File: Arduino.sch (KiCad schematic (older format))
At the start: 16 parts

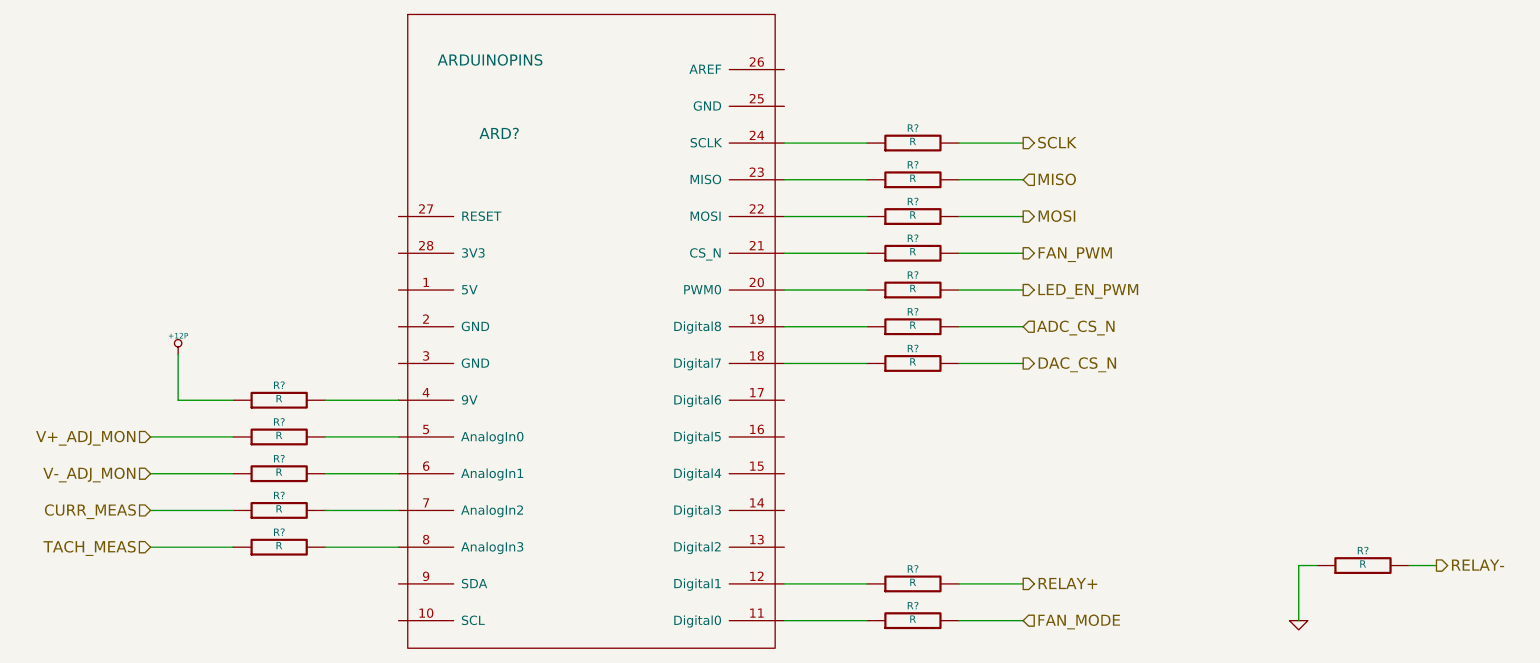
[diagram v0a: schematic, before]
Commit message: Added Relay module footprints.
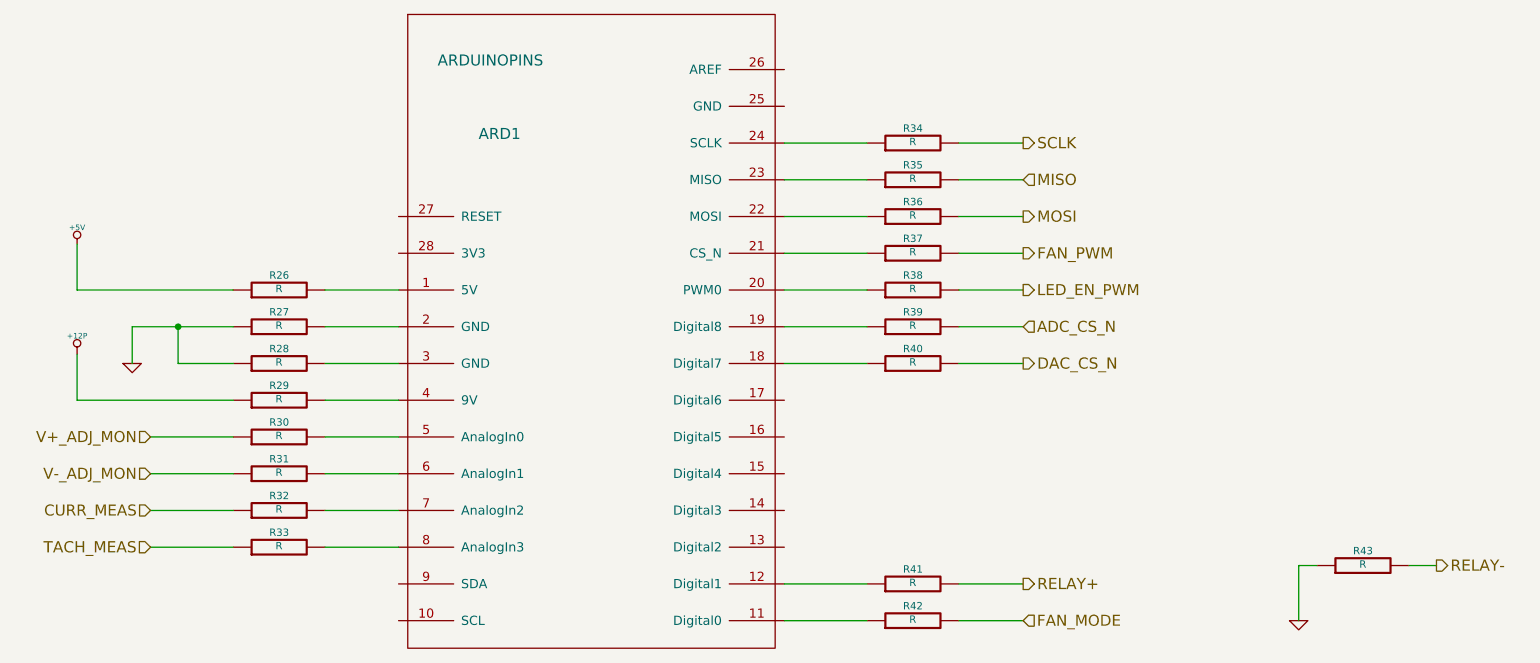
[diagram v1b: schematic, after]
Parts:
- added R26, R27, R28: R, symbol R
- gave numbers to parts that had none: 16
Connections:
- net GND: now also R27.1, R28.1
- net at ARD1.1 (5V): now also R26.2
- net at ARD1.2 (GND): now also R27.2
- net at ARD1.3 (GND): now also R28.2
- new net +5V: R26.1
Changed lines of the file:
@@
 LIBS:valves
 LIBS:BB
+LIBS:GLSP
 LIBS:BB-cache
 EELAYER 24 0
@@
 TACH_MEAS
 $Comp
-L ARDUINOPINS ARD?
+L ARDUINOPINS ARD1
 U 1 1 52F820B7
 P 5000 3950
-F 0 "ARD?" H 4500 5000 60  0000 C CNN
+F 0 "ARD1" H 4500 5000 60  0000 C CNN
 F 1 "ARDUINOPINS" H 4450 5400 60  0000 C CNN
 F 2 "" H 5800 2900 60  0000 C CNN
@@
 CURR_MEAS
 $Comp
-L R R?
+L R R37
 U 1 1 52F82104
 P 6750 3550
-F 0 "R?" V 6830 3550 40  0000 C CNN
+F 0 "R37" V 6830 3550 40  0000 C CNN
 F 1 "R" V 6757 3551 40  0000 C CNN
 F 2 "" V 6680 3550 30  0000 C CNN
@@
 	6500 3550 6050 3550
 $Comp
-L R R?
+L R R41
 U 1 1 52F8212B
 P 6750 5350
-F 0 "R?" V 6830 5350 40  0000 C CNN
+F 0 "R41" V 6830 5350 40  0000 C CNN
 F 1 "R" V 6757 5351 40  0000 C CNN
 F 2 "" V 6680 5350 30  0000 C CNN
@@
 	8850 5250 8850 5550
 $Comp
-L GND #PWR?
+L GND #PWR55
 U 1 1 52F82BF8
 P 8850 5550
-F 0 "#PWR?" H 8850 5550 30  0001 C CNN
+F 0 "#PWR55" H 8850 5550 30  0001 C CNN
 F 1 "GND" H 8850 5480 30  0001 C CNN
 F 2 "" H 8850 5550 60  0000 C CNN
@@
 $EndComp
 $Comp
-L R R?
+L R R33
 U 1 1 52F82E67
 P 3300 5150
-F 0 "R?" V 3380 5150 40  0000 C CNN
+F 0 "R33" V 3380 5150 40  0000 C CNN
 F 1 "R" V 3307 5151 40  0000 C CNN
 F 2 "" V 3230 5150 30  0000 C CNN
@@
 $EndComp
 $Comp
-L R R?
+L R R32
 U 1 1 52F82E72
 P 3300 4950
-F 0 "R?" V 3380 4950 40  0000 C CNN
+F 0 "R32" V 3380 4950 40  0000 C CNN
 F 1 "R" V 3307 4951 40  0000 C CNN
 F 2 "" V 3230 4950 30  0000 C CNN
@@
 V-_ADJ_MON
 $Comp
-L R R?
+L R R31
 U 1 1 52F83112
 P 3300 4750
-F 0 "R?" V 3380 4750 40  0000 C CNN
+F 0 "R31" V 3380 4750 40  0000 C CNN
 F 1 "R" V 3307 4751 40  0000 C CNN
 F 2 "" V 3230 4750 30  0000 C CNN
@@
 $EndComp
 $Comp
-L R R?
+L R R30
 U 1 1 52F8311D
 P 3300 4550
-F 0 "R?" V 3380 4550 40  0000 C CNN
+F 0 "R30" V 3380 4550 40  0000 C CNN
 F 1 "R" V 3307 4551 40  0000 C CNN
 F 2 "" V 3230 4550 30  0000 C CNN
@@
 	2600 4550 3050 4550
 $Comp
-L R R?
+L R R40
 U 1 1 52F833CB
 P 6750 4150
-F 0 "R?" V 6830 4150 40  0000 C CNN
+F 0 "R40" V 6830 4150 40  0000 C CNN
 F 1 "R" V 6757 4151 40  0000 C CNN
 F 2 "" V 6680 4150 30  0000 C CNN
@@
 $EndComp
 $Comp
-L R R?
+L R R36
 U 1 1 52F833D6
 P 6750 3350
-F 0 "R?" V 6830 3350 40  0000 C CNN
+F 0 "R36" V 6830 3350 40  0000 C CNN
 F 1 "R" V 6757 3351 40  0000 C CNN
 F 2 "" V 6680 3350 30  0000 C CNN
@@
 $EndComp
 $Comp
-L R R?
+L R R35
 U 1 1 52F833E1
 P 6750 3150
-F 0 "R?" V 6830 3150 40  0000 C CNN
+F 0 "R35" V 6830 3150 40  0000 C CNN
 F 1 "R" V 6757 3151 40  0000 C CNN
 F 2 "" V 6680 3150 30  0000 C CNN
@@
 $EndComp
 $Comp
-L R R?
+L R R34
 U 1 1 52F833EC
 P 6750 2950
-F 0 "R?" V 6830 2950 40  0000 C CNN
+F 0 "R34" V 6830 2950 40  0000 C CNN
 F 1 "R" V 6757 2951 40  0000 C CNN
 F 2 "" V 6680 2950 30  0000 C CNN
@@
 	6500 4150 6050 4150
 $Comp
-L R R?
+L R R43
 U 1 1 52F83493
 P 9200 5250
-F 0 "R?" V 9280 5250 40  0000 C CNN
+F 0 "R43" V 9280 5250 40  0000 C CNN
 F 1 "R" V 9207 5251 40  0000 C CNN
 F 2 "" V 9130 5250 30  0000 C CNN
@@
 LED_EN_PWM
 $Comp
-L R R?
+L R R38
 U 1 1 52F834CE
 P 6750 3750
-F 0 "R?" V 6830 3750 40  0000 C CNN
+F 0 "R38" V 6830 3750 40  0000 C CNN
 F 1 "R" V 6757 3751 40  0000 C CNN
 F 2 "" V 6680 3750 30  0000 C CNN
@@
 ADC_CS_N
 $Comp
-L R R?
+L R R39
 U 1 1 52F876A6
 P 6750 3950
-F 0 "R?" V 6830 3950 40  0000 C CNN
+F 0 "R39" V 6830 3950 40  0000 C CNN
 F 1 "R" V 6757 3951 40  0000 C CNN
 F 2 "" V 6680 3950 30  0000 C CNN
@@
 FAN_MODE
 $Comp
-L R R?
+L R R42
 U 1 1 52FA1F4F
 P 6750 5550
-F 0 "R?" V 6830 5550 40  0000 C CNN
+F 0 "R42" V 6830 5550 40  0000 C CNN
 F 1 "R" V 6757 5551 40  0000 C CNN
 F 2 "" V 6680 5550 30  0000 C CNN
@@
 	6500 5550 6050 5550
 $Comp
-L R R?
+L R R29
 U 1 1 52FA21F2
 P 3300 4350
-F 0 "R?" V 3380 4350 40  0000 C CNN
+F 0 "R29" V 3380 4350 40  0000 C CNN
 F 1 "R" V 3307 4351 40  0000 C CNN
 F 2 "" V 3230 4350 30  0000 C CNN
@@
 	3950 4350 3550 4350
 $Comp
-L +12P #PWR?
+L +12P #PWR53
 U 1 1 52FA221E
-P 2750 4100
-F 0 "#PWR?" H 2750 4070 30  0001 C CNN
-F 1 "+12P" H 2750 4200 30  0000 C CNN
-F 2 "" H 2750 4100 60  0000 C CNN
-F 3 "" H 2750 4100 60  0000 C CNN
-	1    2750 4100
-	1    0    0    -1
-$EndComp
-Wire Wire Line
-	3050 4350 2750 4350
-Wire Wire Line
-	2750 4350 2750 4100
+P 2200 4100
+F 0 "#PWR53" H 2200 4070 30  0001 C CNN
+F 1 "+12P" H 2200 4200 30  0000 C CNN
+F 2 "" H 2200 4100 60  0000 C CNN
+F 3 "" H 2200 4100 60  0000 C CNN
+	1    2200 4100
+	1    0    0    -1
+$EndComp
+Wire Wire Line
+	3050 4350 2200 4350
+Wire Wire Line
+	2200 4350 2200 4100
+$Comp
+L R R28
+U 1 1 530266F7
+P 3300 4150
+F 0 "R28" V 3380 4150 40  0000 C CNN
+F 1 "R" V 3307 4151 40  0000 C CNN
+F 2 "" V 3230 4150 30  0000 C CNN
+F 3 "" H 3300 4150 30  0000 C CNN
+	1    3300 4150
+	0    -1   -1   0
+$EndComp
+$Comp
+L R R27
+U 1 1 53026702
+P 3300 3950
+F 0 "R27" V 3380 3950 40  0000 C CNN
+F 1 "R" V 3307 3951 40  0000 C CNN
+F 2 "" V 3230 3950 30  0000 C CNN
+F 3 "" H 3300 3950 30  0000 C CNN
+	1    3300 3950
+	0    -1   -1   0
+$EndComp
+$Comp
+L R R26
+U 1 1 5302670D
+P 3300 3750
+F 0 "R26" V 3380 3750 40  0000 C CNN
+F 1 "R" V 3307 3751 40  0000 C CNN
+F 2 "" V 3230 3750 30  0000 C CNN
+F 3 "" H 3300 3750 30  0000 C CNN
+	1    3300 3750
+	0    -1   -1   0
+$EndComp
+Wire Wire Line
+	3950 4150 3550 4150
+Wire Wire Line
+	3950 3950 3550 3950
+Wire Wire Line
+	3950 3750 3550 3750
+Wire Wire Line
+	3050 3750 2200 3750
+Wire Wire Line
+	2200 3750 2200 3500
+$Comp
+L +5V #PWR52
+U 1 1 530267AB
+P 2200 3500
+F 0 "#PWR52" H 2200 3590 20  0001 C CNN
+F 1 "+5V" H 2200 3590 30  0000 C CNN
+F 2 "" H 2200 3500 60  0000 C CNN
+F 3 "" H 2200 3500 60  0000 C CNN
+	1    2200 3500
+	1    0    0    -1
+$EndComp
+Wire Wire Line
+	3050 3950 2500 3950
+Wire Wire Line
+	2500 3950 2500 4150
+$Comp
+L GND #PWR54
+U 1 1 5302681A
+P 2500 4150
+F 0 "#PWR54" H 2500 4150 30  0001 C CNN
+F 1 "GND" H 2500 4080 30  0001 C CNN
+F 2 "" H 2500 4150 60  0000 C CNN
+F 3 "" H 2500 4150 60  0000 C CNN
+	1    2500 4150
+	1    0    0    -1
+$EndComp
+Wire Wire Line
+	3050 4150 2750 4150
+Wire Wire Line
+	2750 4150 2750 3950
+Connection ~ 2750 3950
 $EndSCHEMATC

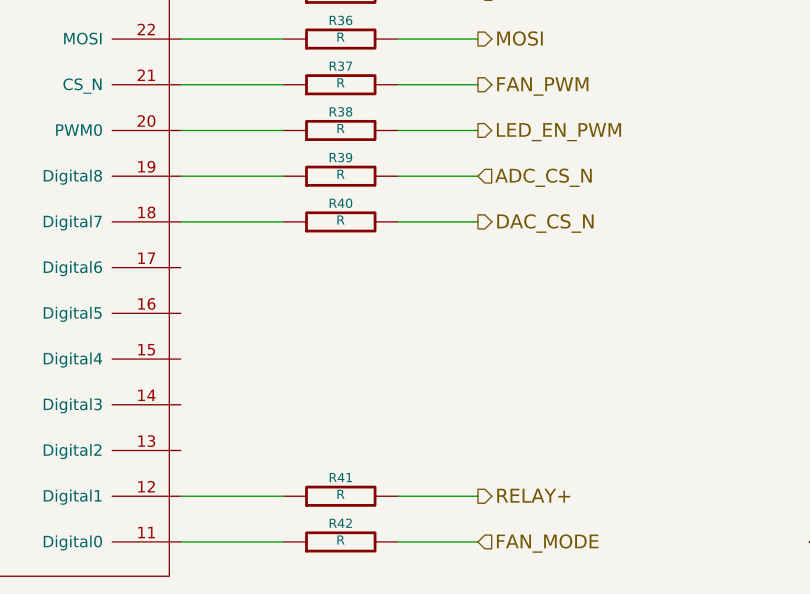
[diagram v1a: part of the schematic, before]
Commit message: Associated and placed thermocouple, terminal, arduino, fan driver, power protection modules.
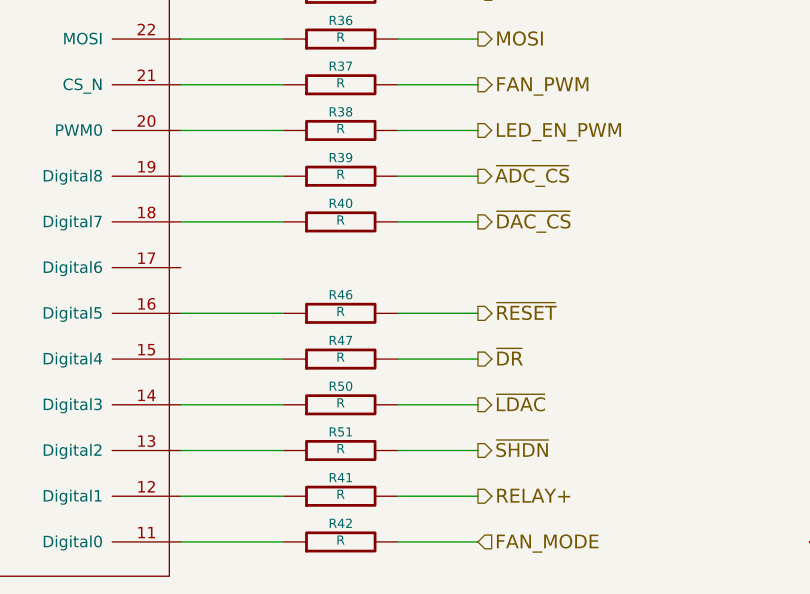
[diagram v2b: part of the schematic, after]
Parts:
- added R46, R47, R50, R51: R, symbol R
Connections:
- net at ARD1.13 (Digital2): now also R51.1
- net at ARD1.14 (Digital3): now also R50.1
- net at ARD1.15 (Digital4): now also R47.1
- net at ARD1.16 (Digital5): now also R46.1
- net ADC_CS_N renamed ~ADC_CS
- net DAC_CS_N renamed ~DAC_CS
- new net ~DR: R47.2
- new net ~LDAC: R50.2
- new net ~RESET: R46.2
- new net ~SHDN: R51.2
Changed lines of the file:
@@
 $Descr A4 11693 8268
 encoding utf-8
-Sheet 9 9
+Sheet 6 9
 Title ""
 Date ""
@@
 SCLK
 Text HLabel 7350 4150 2    61   Output ~ 0
-DAC_CS_N
+~DAC_CS
 Text HLabel 7350 3550 2    61   Output ~ 0
 FAN_PWM
@@
 	8850 5250 8850 5550
 $Comp
-L GND #PWR55
+L GND #PWR048
 U 1 1 52F82BF8
 P 8850 5550
-F 0 "#PWR55" H 8850 5550 30  0001 C CNN
+F 0 "#PWR048" H 8850 5550 30  0001 C CNN
 F 1 "GND" H 8850 5480 30  0001 C CNN
 F 2 "" H 8850 5550 60  0000 C CNN
@@
 Wire Wire Line
 	6500 3750 6050 3750
-Text HLabel 7350 3950 2    60   Input ~ 0
-ADC_CS_N
+Text HLabel 7350 3950 2    60   Output ~ 0
+~ADC_CS
 $Comp
 L R R39
@@
 	3950 4350 3550 4350
 $Comp
-L +12P #PWR53
+L +12P #PWR049
 U 1 1 52FA221E
 P 2200 4100
-F 0 "#PWR53" H 2200 4070 30  0001 C CNN
+F 0 "#PWR049" H 2200 4070 30  0001 C CNN
 F 1 "+12P" H 2200 4200 30  0000 C CNN
 F 2 "" H 2200 4100 60  0000 C CNN
@@
 	2200 3750 2200 3500
 $Comp
-L +5V #PWR52
+L +5V #PWR050
 U 1 1 530267AB
 P 2200 3500
-F 0 "#PWR52" H 2200 3590 20  0001 C CNN
+F 0 "#PWR050" H 2200 3590 20  0001 C CNN
 F 1 "+5V" H 2200 3590 30  0000 C CNN
 F 2 "" H 2200 3500 60  0000 C CNN
@@
 	2500 3950 2500 4150
 $Comp
-L GND #PWR54
+L GND #PWR051
 U 1 1 5302681A
 P 2500 4150
-F 0 "#PWR54" H 2500 4150 30  0001 C CNN
+F 0 "#PWR051" H 2500 4150 30  0001 C CNN
 F 1 "GND" H 2500 4080 30  0001 C CNN
 F 2 "" H 2500 4150 60  0000 C CNN
@@
 	2750 4150 2750 3950
 Connection ~ 2750 3950
+Text HLabel 7350 4550 2    61   Output ~ 0
+~RESET
+$Comp
+L R R46
+U 1 1 53062429
+P 6750 4550
+F 0 "R46" V 6830 4550 40  0000 C CNN
+F 1 "R" V 6757 4551 40  0000 C CNN
+F 2 "" V 6680 4550 30  0000 C CNN
+F 3 "" H 6750 4550 30  0000 C CNN
+	1    6750 4550
+	0    -1   -1   0
+$EndComp
+Wire Wire Line
+	7350 4550 7000 4550
+Wire Wire Line
+	6500 4550 6050 4550
+Text HLabel 7350 4750 2    61   Output ~ 0
+~DR
+$Comp
+L R R47
+U 1 1 53062432
+P 6750 4750
+F 0 "R47" V 6830 4750 40  0000 C CNN
+F 1 "R" V 6757 4751 40  0000 C CNN
+F 2 "" V 6680 4750 30  0000 C CNN
+F 3 "" H 6750 4750 30  0000 C CNN
+	1    6750 4750
+	0    -1   -1   0
+$EndComp
+Wire Wire Line
+	7350 4750 7000 4750
+Wire Wire Line
+	6500 4750 6050 4750
+$Comp
+L R R50
+U 1 1 530A408D
+P 6750 4950
+F 0 "R50" V 6830 4950 40  0000 C CNN
+F 1 "R" V 6757 4951 40  0000 C CNN
+F 2 "" V 6680 4950 30  0000 C CNN
+F 3 "" H 6750 4950 30  0000 C CNN
+	1    6750 4950
+	0    -1   -1   0
+$EndComp
+$Comp
+L R R51
+U 1 1 530A4098
+P 6750 5150
+F 0 "R51" V 6830 5150 40  0000 C CNN
+F 1 "R" V 6757 5151 40  0000 C CNN
+F 2 "" V 6680 5150 30  0000 C CNN
+F 3 "" H 6750 5150 30  0000 C CNN
+	1    6750 5150
+	0    -1   -1   0
+$EndComp
+Text HLabel 7350 4950 2    60   Output ~ 0
+~LDAC
+Text HLabel 7350 5150 2    60   Output ~ 0
+~SHDN
+Wire Wire Line
+	6050 4950 6500 4950
+Wire Wire Line
+	6050 5150 6500 5150
+Wire Wire Line
+	7000 4950 7350 4950
+Wire Wire Line
+	7000 5150 7350 5150
 $EndSCHEMATC
